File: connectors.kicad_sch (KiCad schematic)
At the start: 13 parts, among them J1 USB-C_DX07S024JJ2, J2 PCIe_x4_Conn_EdgeMount_Open, J3 Conn_Molex_NanoFit_1053131202

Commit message: [#58582] Globlib
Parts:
- C1, C6: footprint thunderbolt-pcie-adapter-footprints:C_0805_2012Metric -> antmicro-footprints:C_0805_2012Metric; symbol thunderbolt-pcie-adapter:C_10u_0805_35V -> antmicroCapacitorsmisc:C_10u_0805_35V
- C2, C3, C4, C5: footprint thunderbolt-pcie-adapter-footprints:C_0402_1005Metric -> antmicro-footprints:C_0402_1005Metric; symbol thunderbolt-pcie-adapter:C_100n_0402 -> antmicroCapacitors0402:C_100n_0402
- J1: footprint thunderbolt-pcie-adapter-footprints:USB-3.1-Gen2_Type-C_JAE_DX07S024JJ2_Horizontal -> antmicro-footprints:USB-C_Receptacle_JAE_DX07S024JJ2; symbol thunderbolt-pcie-adapter:USB-C_DX07S024JJ2 -> antmicroUSBConnectors:USB-C_JAE_DX07S024JJ2
- J2: footprint thunderbolt-pcie-adapter-footprints:PCIE_TE_2-2387405-2 -> antmicro-footprints:PCIE_TE_2-2387405-2; symbol thunderbolt-pcie-adapter:PCIe_x4_Conn_EdgeMount_Open -> antmicroPciConnectors:PCIe_x4_Conn_EdgeMount_Open
- R1: footprint thunderbolt-pcie-adapter-footprints:R_0402_1005Metric -> antmicro-footprints:R_0402_1005Metric; symbol thunderbolt-pcie-adapter:R_3k3_0402 -> antmicroResistors0402:R_3k3_0402

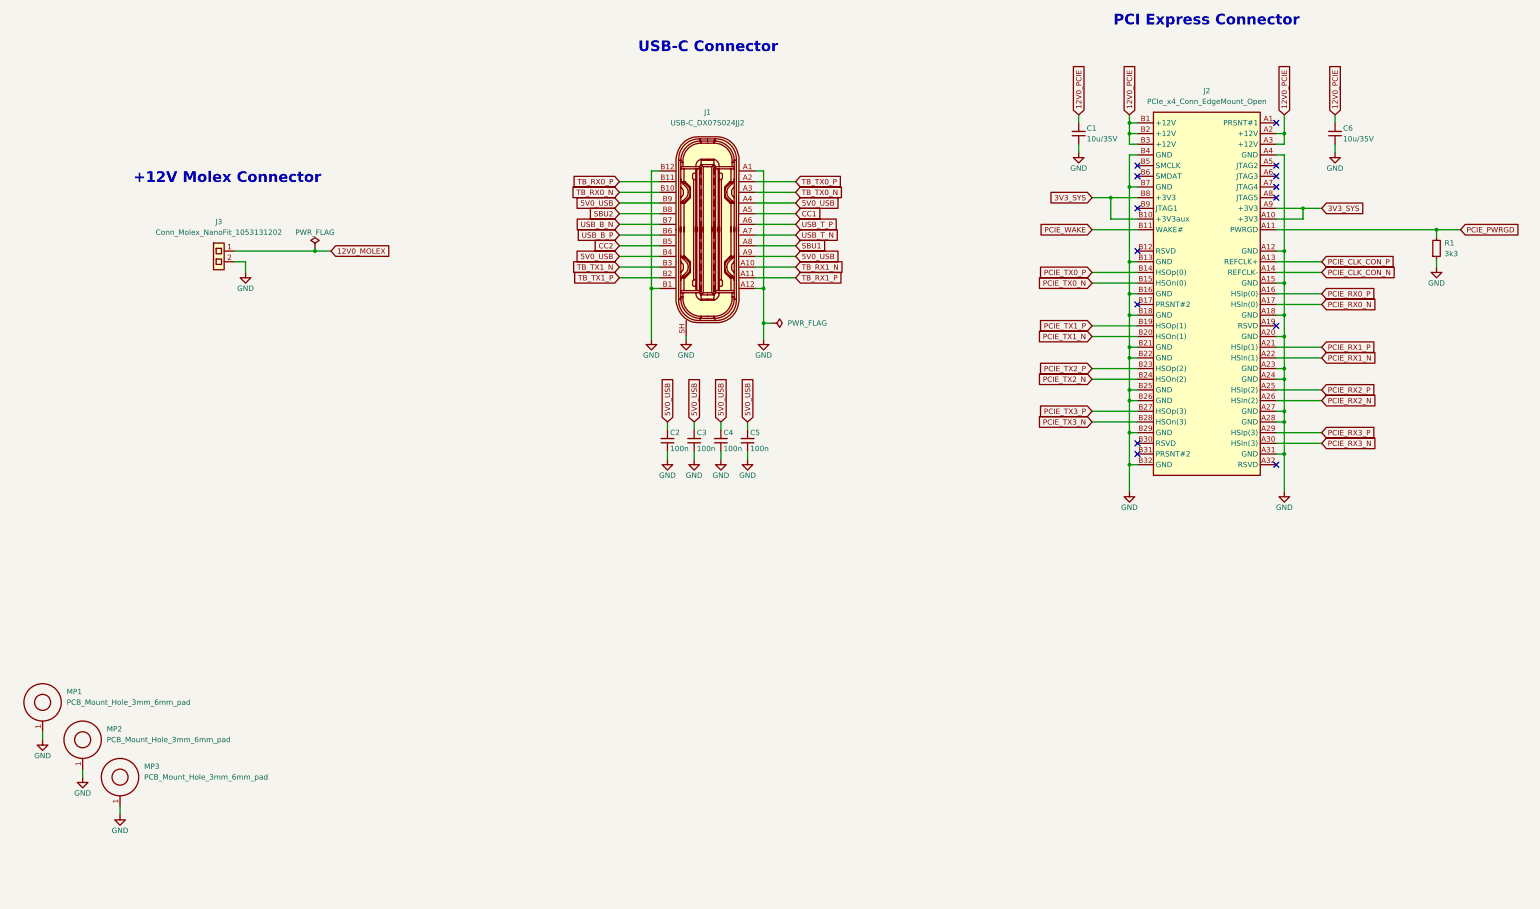
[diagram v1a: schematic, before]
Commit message: [#58582] WiP: Update symbols to global
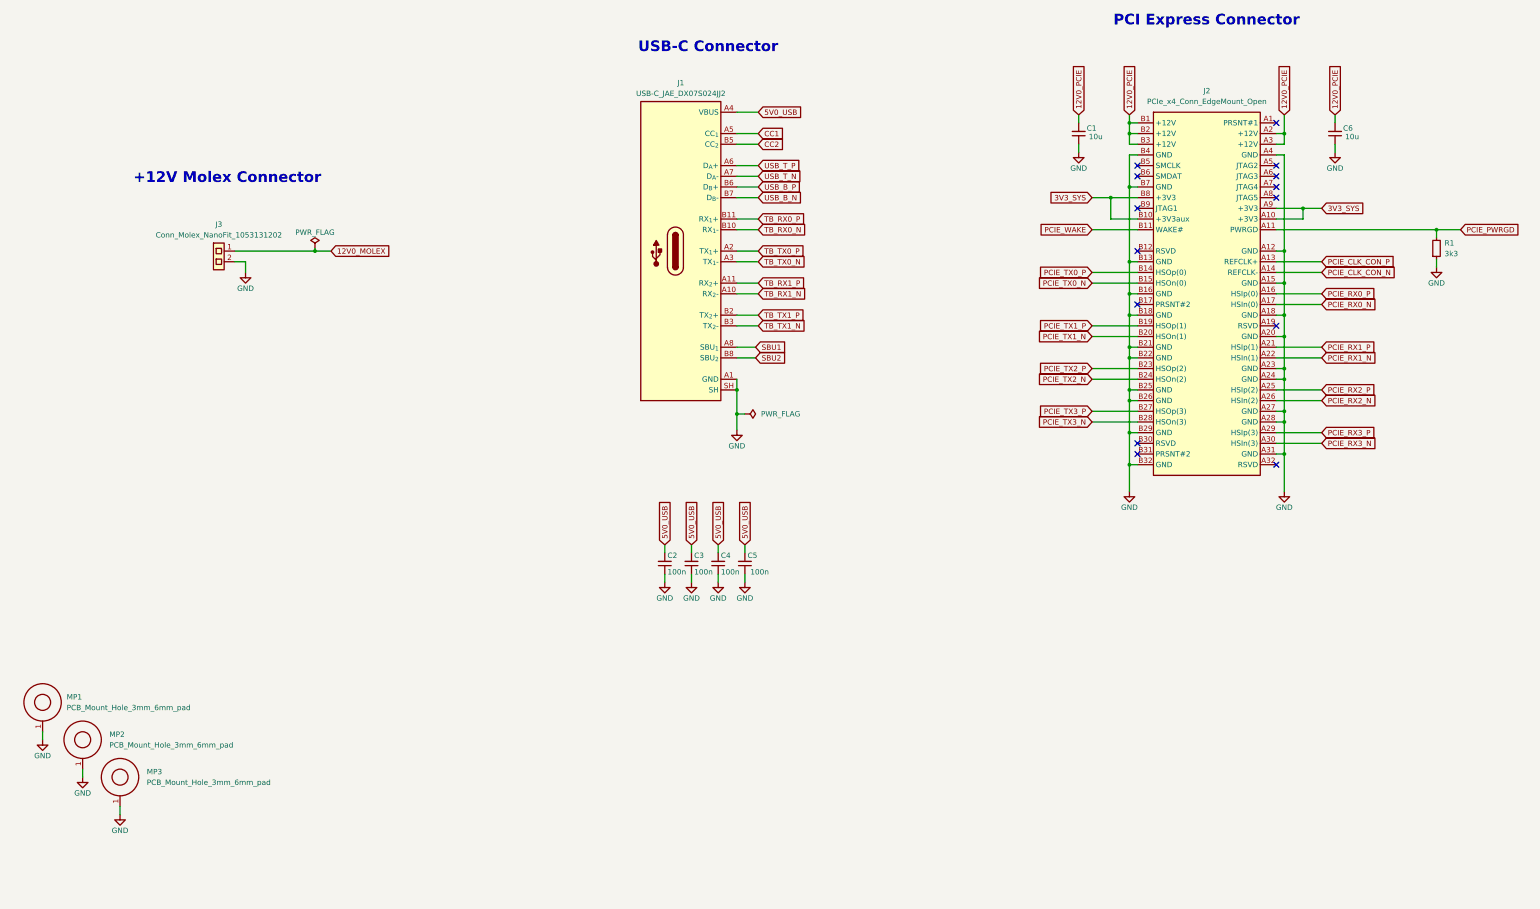
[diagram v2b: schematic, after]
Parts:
- C1, C6: Val 10u/35V -> 10u; Voltage (none) -> 35V
- J1: value USB-C_DX07S024JJ2 -> USB-C_JAE_DX07S024JJ2
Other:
- moved on the sheet: C2, C3, C4, C5

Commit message: [#58582] Update GND to global
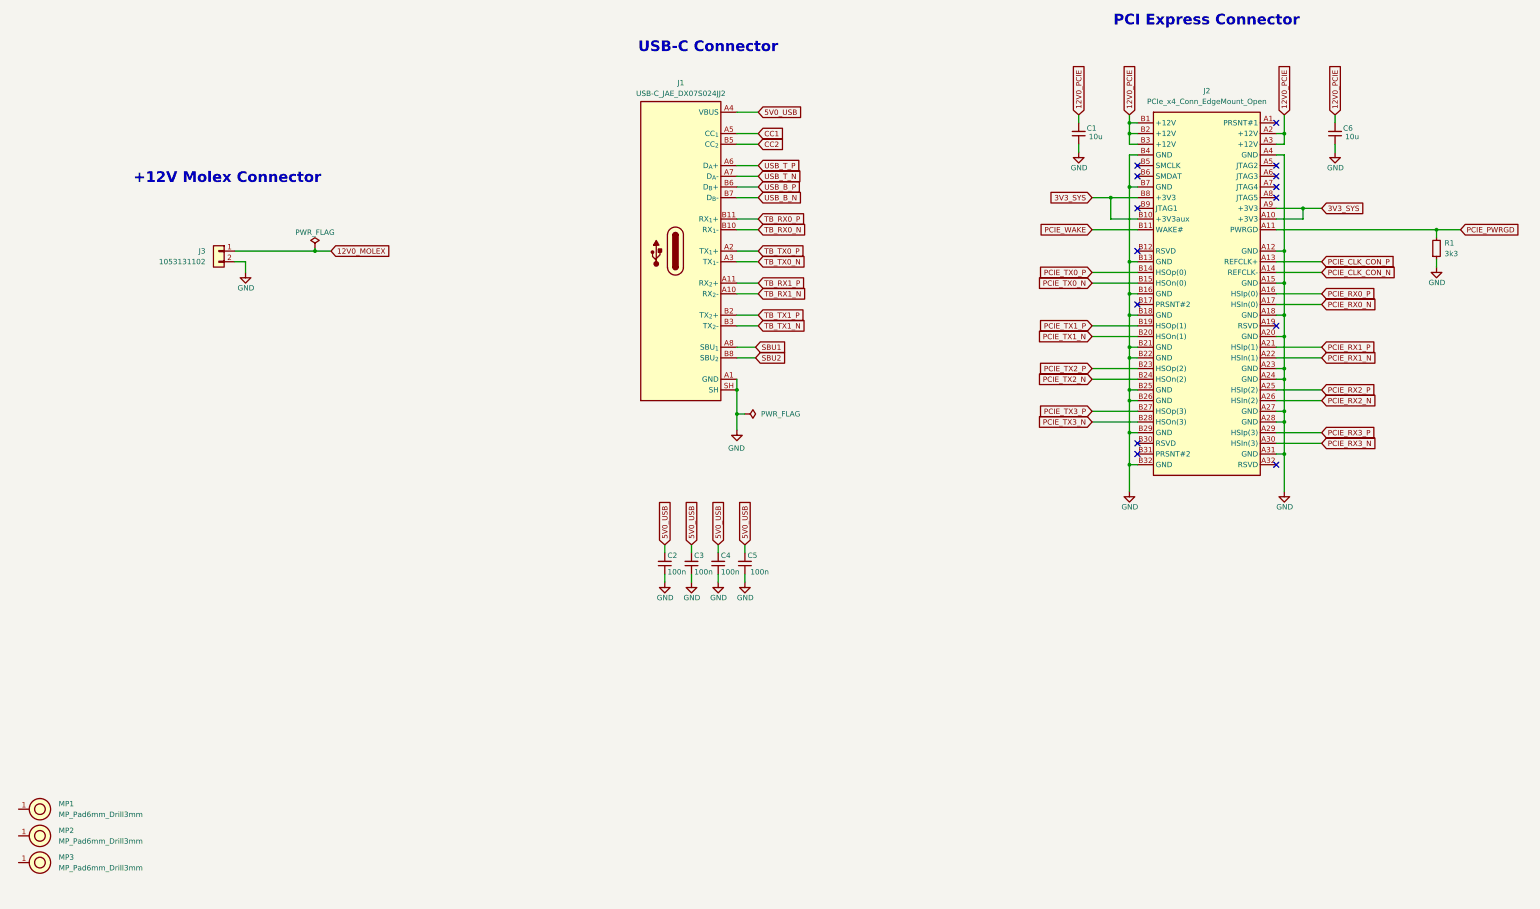
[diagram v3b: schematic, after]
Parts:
- removed J3: Conn_Molex_NanoFit_1053131202, thunderbolt-pcie-adapter-footprints:Conn_Molex_NanoFit_1053131202, symbol thunderbolt-pcie-adapter:Conn_Molex_NanoFit_1053131202
- removed MP1, MP2, MP3: PCB_Mount_Hole_3mm_6mm_pad, thunderbolt-pcie-adapter-footprints:mounting-hole-3.2mm, symbol thunderbolt-pcie-adapter:PCB_Mount_Hole_3mm_6mm_pad
- added J3: Molex_Nano-Fit_1x2_1053131102, antmicro-footprints:Conn_Molex_Nano-Fit_1x2_1053131102, symbol antmicroWire2BoardConnectors:Molex_Nano-Fit_1x2_1053131102
- added MP1, MP2, MP3: MP_Pad6mm_Drill3mm, antmicro-footprints:MP_Pad6mm_Drill3mm, symbol antmicroMechanicalParts:MP_Pad6mm_Drill3mm
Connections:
- net 12V0_MOLEX: now also J3.1
- net GND: now also J3.2

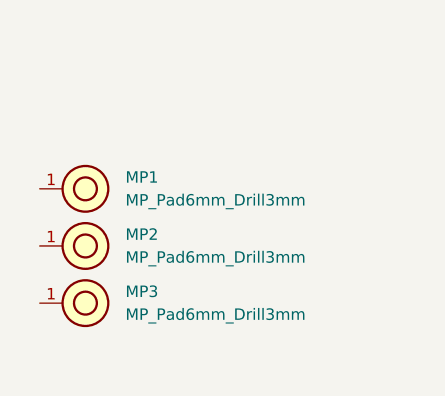
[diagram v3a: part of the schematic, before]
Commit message: [#58582] Clean ERC
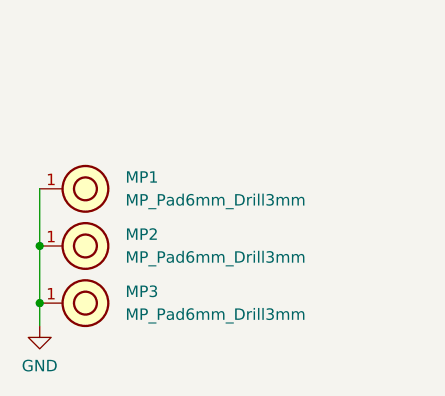
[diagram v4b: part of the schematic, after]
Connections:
- net GND: now also MP1.1, MP2.1, MP3.1
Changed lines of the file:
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@@
   (junction (at 331.47 151.13) (diameter 0) (color 0 0 0 0)
   )
+  (junction (at 30.48 269.875) (diameter 0) (color 0 0 0 0)
+  )
   (junction (at 201.295 163.83) (diameter 0) (color 0 0 0 0)
   )
   (junction (at 331.47 102.87) (diameter 0) (color 0 0 0 0)
+  )
+  (junction (at 30.48 276.225) (diameter 0) (color 0 0 0 0)
   )
   (junction (at 331.47 146.05) (diameter 0) (color 0 0 0 0)
@@
     (stroke (width 0) (type default))
   )
+  (wire (pts (xy 30.48 276.225) (xy 30.48 278.765))
+    (stroke (width 0) (type default))
+  )
   (wire (pts (xy 84.455 135.89) (xy 84.455 133.35))
     (stroke (width 0) (type default))
@@
     (stroke (width 0) (type default))
   )
+  (wire (pts (xy 30.48 269.875) (xy 30.48 276.225))
+    (stroke (width 0) (type default))
+  )
   (wire (pts (xy 294.64 173.99) (xy 294.64 181.61))
     (stroke (width 0) (type default))
@@
   )
   (wire (pts (xy 201.295 110.49) (xy 206.375 110.49))
+    (stroke (width 0) (type default))
+  )
+  (wire (pts (xy 30.48 263.525) (xy 30.48 269.875))
     (stroke (width 0) (type default))
   )
@@
         )
       )
+    )
+  )
+  (symbol (lib_id "antmicropower:GND") (at 30.48 278.765 0) (unit 1)
+    (in_bom yes) (on_board yes) (dnp no) (fields_autoplaced)
+    (property "Reference" "#PWR03" (at 39.37 281.305 0)
+      (effects (font (size 1.27 1.27) (thickness 0.15)) (justify left bottom) hide)
+    )
+    (property "Value" "GND" (at 30.48 283.21 0)
+      (effects (font (size 1.27 1.27) (thickness 0.15)))
+    )
+    (property "Footprint" "" (at 39.37 286.385 0)
+      (effects (font (size 1.27 1.27) (thickness 0.15)) (justify left bottom) hide)
+    )
+    (property "Datasheet" "" (at 39.37 291.465 0)
+      (effects (font (size 1.27 1.27) (thickness 0.15)) (justify left bottom) hide)
+    )
+    (property "Author" "Antmicro" (at 39.37 286.385 0)
+      (effects (font (size 1.27 1.27) (thickness 0.15)) (justify left bottom) hide)
+    )
+    (property "License" "Apache-2.0" (at 39.37 288.925 0)
+      (effects (font (size 1.27 1.27) (thickness 0.15)) (justify left bottom) hide)
+    )
+    (pin "1")
+    (instances
+      (project "thunderbolt-pcie-adapter"
+        (path "/6701ed44-03d2-4633-acc7-b19b85d75ead/3cf1056a-c882-4aa3-b4ed-cc5a76fc7bf3"
+          (reference "#PWR03") (unit 1)
+        )
+      )
